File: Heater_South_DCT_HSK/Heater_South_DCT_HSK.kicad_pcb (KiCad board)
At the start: 2 copper layers, 53.3 x 63.5 mm, 8 parts, among them J1 SHB1, J2 SHB2, J3 Heater South

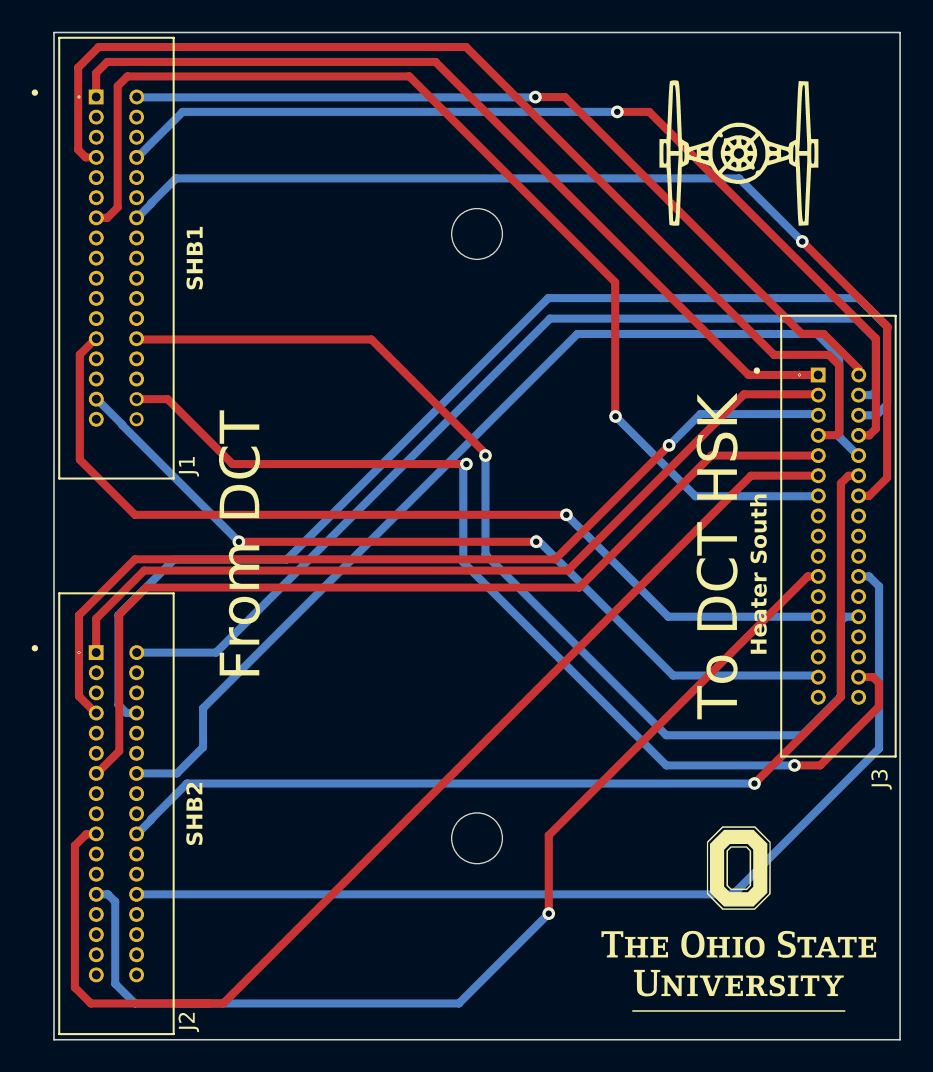
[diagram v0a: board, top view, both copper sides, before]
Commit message: New feedthrough PCBs to access spare heater channels for flowcontroller heaters.
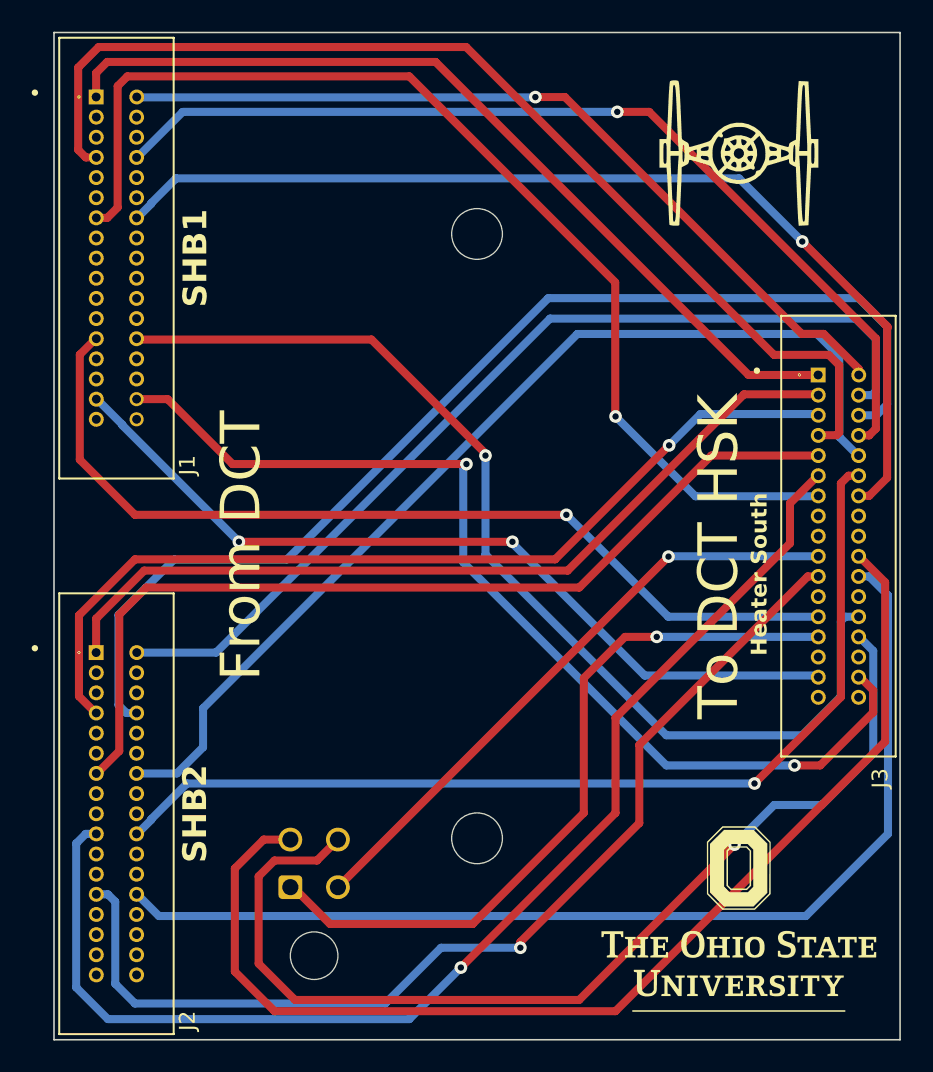
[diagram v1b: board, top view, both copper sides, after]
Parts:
- added J4: SparesS, Connector_Molex:Molex_Micro-Fit_3.0_43045-0400_2x02_P3.00mm_Horizontal, B.Cu at (116.5, 104.7)
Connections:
- J3 pad 19: unconnected-(J3-Pin_19-Pad19) -> /SpareS1+
- J3 pad 20: unconnected-(J3-Pin_20-Pad20) -> /SpareS1-
- J3 pad 27: unconnected-(J3-Pin_27-Pad27) -> /SpareS2+
- J3 pad 28: unconnected-(J3-Pin_28-Pad28) -> /SpareS2-
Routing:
- net /SpareS1-: track 0.00 -> 72.2 mm
- net /SpareS2-: track 0.00 -> 65.4 mm, vias 0 -> 1
- net /SpareS2+: track 0.00 -> 46.7 mm, vias 0 -> 1
- net /SpareS1+: track 0.00 -> 38.9 mm, vias 0 -> 1
- net /HB2_26: track 62.4 -> 67.5 mm
- net /HB2_19: track 73.8 -> 77.4 mm, vias 0 -> 1
- net /HB1_32: track 64.6 -> 63.9 mm

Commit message: Files fabbed and tested. These work for the new version of the heater driver PCB.
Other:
- board text added: "Heater South Rev C Dennis H. Calderon 10/17/2023"
- board text removed: "Heater South Rev B Dennis H. Calderon 09/09/2023"
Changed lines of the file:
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@@
       (drillshape 0)
       (scaleselection 1)
-      (outputdirectory "Fab/Rev_B/")
+      (outputdirectory "Fab/Rev_C/")
     )
   )
@@
     (property "ki_keywords" "connector")
     (attr through_hole)
-    (fp_text reference "J4" (at 1.5 10.12) (layer "B.SilkS")
+    (fp_text reference "J4" (at 5 -5.18) (layer "B.SilkS")
         (effects (font (size 1 1) (thickness 0.15)) (justify mirror))
     )
@@
       (stroke (width 0.1) (type solid)) (layer "B.Fab"))
     (pad "" np_thru_hole circle (at 1.5 4.32) (size 3 3) (drill 3) (layers "*.Cu" "*.Mask"))
-    (pad "1" thru_hole roundrect (at 0 0) (size 1.5 1.5) (drill 1.02) (layers "*.Cu" "*.Mask") (roundrect_rratio 0.166667)
+    (pad "1" thru_hole roundrect (at 0 0) (size 1.5 1.5) (drill 1.02) (layers "*.Cu" "*.Mask") (roundrect_rratio 0.1666673333)
       (net 77 "/SpareS2+") (pinfunction "Pin_1") (pintype "passive"))
     (pad "2" thru_hole circle (at 3 0) (size 1.5 1.5) (drill 1.02) (layers "*.Cu" "*.Mask")
@@
     (effects (font (size 3.5 3.5) (thickness 0.5)) (justify right bottom mirror))
   )
-  (gr_text "Heater South Rev B\nDennis H. Calderon\n09/09/2023" (at 144.772052 106.686389) (layer "B.SilkS")
+  (gr_text "Heater South Rev C\nDennis H. Calderon\n10/17/2023" (at 144.772052 106.686389) (layer "B.SilkS")
     (effects (font (size 1.3 1.3) (thickness 0.3) bold) (justify mirror))
   )
